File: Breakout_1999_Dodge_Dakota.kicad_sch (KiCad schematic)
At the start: 583 parts, among them J1 Dodge_Con, U1 ACS712xLCTR-20A

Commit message: Another draft check in. Deleted unused "export" files.
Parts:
- removed F10, F11, F12, F13, F14, F15, F16, F17, F18, F19, F20, F21, F22, F23, F24, F25, F26, F27, F28, F29, F30, F31, F32, F33, F34, F35, F36, F37, F38, F39, F4, F40, F41, F42, F43, F44, F45, F46, F47, F48, F49, F5, F50, F51, F52, F53, F54, F55, F56, F57, F58, F59, F6, F60, F61, F62, F63, F64, F65, F66, F67, F68, F69, F7, F70, F71, F72, F73, F74, F75, F76, F77, F78, F79, F8, F80, F81, F82, F83, F84, F85, F86, F87, F88, F89, F9, F90, F91, F92, F93, F94, F95, F96: Fuse_Holder, LCSC_parts:LCSC_C492610_Fuse_holder, symbol Device:R_Small
- removed TP10, TP11, TP12, TP13, TP14, TP15, TP16, TP17, TP18, TP19, TP20, TP21, TP22, TP23, TP24, TP25, TP26, TP27, TP28, TP29, TP30, TP31, TP32, TP33, TP34, TP35, TP36, TP37, TP38, TP39, TP4, TP40, TP41, TP42, TP43, TP44, TP45, TP46, TP47, TP48, TP49, TP5, TP50, TP51, TP52, TP53, TP54, TP55, TP56, TP57, TP58, TP59, TP6, TP60, TP61, TP62, TP63, TP64, TP65, TP66, TP67, TP68, TP69, TP7, TP70, TP71, TP72, TP73, TP74, TP75, TP76, TP77, TP78, TP79, TP8, TP80, TP81, TP82, TP83, TP84, TP85, TP86, TP87, TP88, TP89, TP9, TP90, TP91, TP92, TP93, TP94, TP95, TP96: TestPoint_2Pole, TestPoint:TestPoint_2Pads_Pitch5.08mm_Drill1.3mm, symbol Connector:TestPoint_2Pole
- added F104, F105, F106, F107, F108, F109, F110, F111, F112, F113, F114, F115, F116, F117, F118, F119, F1193, F1194, F1195, F1196, F1197, F120, F121, F122, F123, F124, F125, F126, F127, F128, F129, F130, F131, F132, F201, F202, F203, F204, F205, F206, F207, F208, F209, F210, F211, F212, F213, F214, F215, F216, F217, F218, F219, F220, F221, F222, F223, F224, F225, F226, F227, F228, F229, F230, F231, F232, F301, F302, F303, F304, F305, F306, F307, F308, F309, F310, F311, F312, F313, F314, F315, F316, F317, F318, F319, F320, F321, F322, F323, F324, F325, F326, F327, F328, F329, F330, F331, F332: Fuse_Holder, LCSC_parts:LCSC_C2935870_Fuse_holder, symbol Device:R_Small
- added F1385, F1386, F1387, F1389, F1391, F1392, F1393, F1394, F1395, F1396, F1397, F1399, F1401, F1402, F1403, F1404, F1405, F1407, F1411, F1413: Pig_Con, TestPoint:TestPoint_THTPad_1.5x1.5mm_Drill0.7mm, symbol Connector:TestPoint
- added TP104, TP105, TP106, TP107, TP108, TP109, TP110, TP111, TP112, TP113, TP114, TP115, TP116, TP117, TP118, TP119, TP120, TP121, TP122, TP123, TP124, TP125, TP126, TP127, TP128, TP129, TP130, TP131, TP132, TP201, TP202, TP203, TP204, TP205, TP206, TP207, TP208, TP209, TP210, TP211, TP212, TP213, TP214, TP215, TP216, TP217, TP218, TP219, TP220, TP221, TP222, TP223, TP224, TP225, TP226, TP227, TP228, TP229, TP230, TP231, TP232, TP301, TP302, TP303, TP304, TP305, TP306, TP307, TP308, TP309, TP310, TP311, TP312, TP313, TP314, TP315, TP316, TP317, TP318, TP319, TP320, TP321, TP322, TP323, TP324, TP325, TP326, TP327, TP328, TP329, TP330, TP331, TP332: TestPoint_2Pole, TestPoint:TestPoint_2Pads_Pitch5.08mm_Drill1.3mm, symbol Connector:TestPoint_2Pole
- added U1, U2, U3, U4, U5: ACS712xLCTR-20A, Package_SO:SOIC-8_3.9x4.9mm_P1.27mm, symbol Sensor_Current:ACS712xLCTR-20A
- F101: renamed from F1; footprint LCSC_parts:LCSC_C492610_Fuse_holder -> LCSC_parts:LCSC_C2935870_Fuse_holder; LCSC C492610 -> C2935870
- F102: renamed from F2; footprint LCSC_parts:LCSC_C492610_Fuse_holder -> LCSC_parts:LCSC_C2935870_Fuse_holder; LCSC C492610 -> C2935870
- F103: renamed from F3; footprint LCSC_parts:LCSC_C492610_Fuse_holder -> LCSC_parts:LCSC_C2935870_Fuse_holder; LCSC C492610 -> C2935870
- F1198: renamed from F385; footprint LCSC_parts:LCSC_C492610_Fuse_holder -> LCSC_parts:LCSC_C2935870_Fuse_holder; LCSC C492610 -> C2935870
- F401: renamed from F97; footprint LCSC_parts:LCSC_C492610_Fuse_holder -> LCSC_parts:LCSC_C2935870_Fuse_holder; LCSC C492610 -> C2935870
- F402: renamed from F98; footprint LCSC_parts:LCSC_C492610_Fuse_holder -> LCSC_parts:LCSC_C2935870_Fuse_holder; LCSC C492610 -> C2935870
- F403: renamed from F99; footprint LCSC_parts:LCSC_C492610_Fuse_holder -> LCSC_parts:LCSC_C2935870_Fuse_holder; LCSC C492610 -> C2935870
- F404: renamed from F100; footprint LCSC_parts:LCSC_C492610_Fuse_holder -> LCSC_parts:LCSC_C2935870_Fuse_holder; LCSC C492610 -> C2935870
- F405: renamed from F101; footprint LCSC_parts:LCSC_C492610_Fuse_holder -> LCSC_parts:LCSC_C2935870_Fuse_holder; LCSC C492610 -> C2935870
- F406: renamed from F102; footprint LCSC_parts:LCSC_C492610_Fuse_holder -> LCSC_parts:LCSC_C2935870_Fuse_holder; LCSC C492610 -> C2935870
- F407: renamed from F103; footprint LCSC_parts:LCSC_C492610_Fuse_holder -> LCSC_parts:LCSC_C2935870_Fuse_holder; LCSC C492610 -> C2935870
- F408: renamed from F104; footprint LCSC_parts:LCSC_C492610_Fuse_holder -> LCSC_parts:LCSC_C2935870_Fuse_holder; LCSC C492610 -> C2935870
- F409: renamed from F105; footprint LCSC_parts:LCSC_C492610_Fuse_holder -> LCSC_parts:LCSC_C2935870_Fuse_holder; LCSC C492610 -> C2935870
- F410: renamed from F106; footprint LCSC_parts:LCSC_C492610_Fuse_holder -> LCSC_parts:LCSC_C2935870_Fuse_holder; LCSC C492610 -> C2935870
- F411: renamed from F107; footprint LCSC_parts:LCSC_C492610_Fuse_holder -> LCSC_parts:LCSC_C2935870_Fuse_holder; LCSC C492610 -> C2935870
- F412: renamed from F108; footprint LCSC_parts:LCSC_C492610_Fuse_holder -> LCSC_parts:LCSC_C2935870_Fuse_holder; LCSC C492610 -> C2935870
- F413: renamed from F109; footprint LCSC_parts:LCSC_C492610_Fuse_holder -> LCSC_parts:LCSC_C2935870_Fuse_holder; LCSC C492610 -> C2935870
- F414: renamed from F110; footprint LCSC_parts:LCSC_C492610_Fuse_holder -> LCSC_parts:LCSC_C2935870_Fuse_holder; LCSC C492610 -> C2935870
- F415: renamed from F111; footprint LCSC_parts:LCSC_C492610_Fuse_holder -> LCSC_parts:LCSC_C2935870_Fuse_holder; LCSC C492610 -> C2935870
- F416: renamed from F112; footprint LCSC_parts:LCSC_C492610_Fuse_holder -> LCSC_parts:LCSC_C2935870_Fuse_holder; LCSC C492610 -> C2935870
- F417: renamed from F113; footprint LCSC_parts:LCSC_C492610_Fuse_holder -> LCSC_parts:LCSC_C2935870_Fuse_holder; LCSC C492610 -> C2935870
- F418: renamed from F114; footprint LCSC_parts:LCSC_C492610_Fuse_holder -> LCSC_parts:LCSC_C2935870_Fuse_holder; LCSC C492610 -> C2935870
- F419: renamed from F115; footprint LCSC_parts:LCSC_C492610_Fuse_holder -> LCSC_parts:LCSC_C2935870_Fuse_holder; LCSC C492610 -> C2935870
- F420: renamed from F116; footprint LCSC_parts:LCSC_C492610_Fuse_holder -> LCSC_parts:LCSC_C2935870_Fuse_holder; LCSC C492610 -> C2935870
- F421: renamed from F117; footprint LCSC_parts:LCSC_C492610_Fuse_holder -> LCSC_parts:LCSC_C2935870_Fuse_holder; LCSC C492610 -> C2935870
- F422: renamed from F118; footprint LCSC_parts:LCSC_C492610_Fuse_holder -> LCSC_parts:LCSC_C2935870_Fuse_holder; LCSC C492610 -> C2935870
- F423: renamed from F119; footprint LCSC_parts:LCSC_C492610_Fuse_holder -> LCSC_parts:LCSC_C2935870_Fuse_holder; LCSC C492610 -> C2935870
- F424: renamed from F120; footprint LCSC_parts:LCSC_C492610_Fuse_holder -> LCSC_parts:LCSC_C2935870_Fuse_holder; LCSC C492610 -> C2935870
- F425: renamed from F121; footprint LCSC_parts:LCSC_C492610_Fuse_holder -> LCSC_parts:LCSC_C2935870_Fuse_holder; LCSC C492610 -> C2935870
- F426: renamed from F122; footprint LCSC_parts:LCSC_C492610_Fuse_holder -> LCSC_parts:LCSC_C2935870_Fuse_holder; LCSC C492610 -> C2935870
- F427: renamed from F123; footprint LCSC_parts:LCSC_C492610_Fuse_holder -> LCSC_parts:LCSC_C2935870_Fuse_holder; LCSC C492610 -> C2935870
- F428: renamed from F124; footprint LCSC_parts:LCSC_C492610_Fuse_holder -> LCSC_parts:LCSC_C2935870_Fuse_holder; LCSC C492610 -> C2935870
- F429: renamed from F125; footprint LCSC_parts:LCSC_C492610_Fuse_holder -> LCSC_parts:LCSC_C2935870_Fuse_holder; LCSC C492610 -> C2935870
- F430: renamed from F126; footprint LCSC_parts:LCSC_C492610_Fuse_holder -> LCSC_parts:LCSC_C2935870_Fuse_holder; LCSC C492610 -> C2935870
- F431: renamed from F127; footprint LCSC_parts:LCSC_C492610_Fuse_holder -> LCSC_parts:LCSC_C2935870_Fuse_holder; LCSC C492610 -> C2935870
- F432: renamed from F128; footprint LCSC_parts:LCSC_C492610_Fuse_holder -> LCSC_parts:LCSC_C2935870_Fuse_holder; LCSC C492610 -> C2935870
- F501: renamed from F129; footprint LCSC_parts:LCSC_C492610_Fuse_holder -> LCSC_parts:LCSC_C2935870_Fuse_holder; LCSC C492610 -> C2935870
- F502: renamed from F130; footprint LCSC_parts:LCSC_C492610_Fuse_holder -> LCSC_parts:LCSC_C2935870_Fuse_holder; LCSC C492610 -> C2935870
- F503: renamed from F131; footprint LCSC_parts:LCSC_C492610_Fuse_holder -> LCSC_parts:LCSC_C2935870_Fuse_holder; LCSC C492610 -> C2935870
- F504: renamed from F132; footprint LCSC_parts:LCSC_C492610_Fuse_holder -> LCSC_parts:LCSC_C2935870_Fuse_holder; LCSC C492610 -> C2935870
- F505: renamed from F133; footprint LCSC_parts:LCSC_C492610_Fuse_holder -> LCSC_parts:LCSC_C2935870_Fuse_holder; LCSC C492610 -> C2935870
- F506: renamed from F134; footprint LCSC_parts:LCSC_C492610_Fuse_holder -> LCSC_parts:LCSC_C2935870_Fuse_holder; LCSC C492610 -> C2935870
- F507: renamed from F135; footprint LCSC_parts:LCSC_C492610_Fuse_holder -> LCSC_parts:LCSC_C2935870_Fuse_holder; LCSC C492610 -> C2935870
- F508: renamed from F136; footprint LCSC_parts:LCSC_C492610_Fuse_holder -> LCSC_parts:LCSC_C2935870_Fuse_holder; LCSC C492610 -> C2935870
- F509: renamed from F137; footprint LCSC_parts:LCSC_C492610_Fuse_holder -> LCSC_parts:LCSC_C2935870_Fuse_holder; LCSC C492610 -> C2935870
- F510: renamed from F138; footprint LCSC_parts:LCSC_C492610_Fuse_holder -> LCSC_parts:LCSC_C2935870_Fuse_holder; LCSC C492610 -> C2935870
- F511: renamed from F139; footprint LCSC_parts:LCSC_C492610_Fuse_holder -> LCSC_parts:LCSC_C2935870_Fuse_holder; LCSC C492610 -> C2935870
- F512: renamed from F140; footprint LCSC_parts:LCSC_C492610_Fuse_holder -> LCSC_parts:LCSC_C2935870_Fuse_holder; LCSC C492610 -> C2935870
- F513: renamed from F141; footprint LCSC_parts:LCSC_C492610_Fuse_holder -> LCSC_parts:LCSC_C2935870_Fuse_holder; LCSC C492610 -> C2935870
- F514: renamed from F142; footprint LCSC_parts:LCSC_C492610_Fuse_holder -> LCSC_parts:LCSC_C2935870_Fuse_holder; LCSC C492610 -> C2935870
- F515: renamed from F143; footprint LCSC_parts:LCSC_C492610_Fuse_holder -> LCSC_parts:LCSC_C2935870_Fuse_holder; LCSC C492610 -> C2935870
- F516: renamed from F144; footprint LCSC_parts:LCSC_C492610_Fuse_holder -> LCSC_parts:LCSC_C2935870_Fuse_holder; LCSC C492610 -> C2935870
- F517: renamed from F145; footprint LCSC_parts:LCSC_C492610_Fuse_holder -> LCSC_parts:LCSC_C2935870_Fuse_holder; LCSC C492610 -> C2935870
- F518: renamed from F146; footprint LCSC_parts:LCSC_C492610_Fuse_holder -> LCSC_parts:LCSC_C2935870_Fuse_holder; LCSC C492610 -> C2935870
- F519: renamed from F147; footprint LCSC_parts:LCSC_C492610_Fuse_holder -> LCSC_parts:LCSC_C2935870_Fuse_holder; LCSC C492610 -> C2935870
- F520: renamed from F148; footprint LCSC_parts:LCSC_C492610_Fuse_holder -> LCSC_parts:LCSC_C2935870_Fuse_holder; LCSC C492610 -> C2935870
- F521: renamed from F149; footprint LCSC_parts:LCSC_C492610_Fuse_holder -> LCSC_parts:LCSC_C2935870_Fuse_holder; LCSC C492610 -> C2935870
- F522: renamed from F150; footprint LCSC_parts:LCSC_C492610_Fuse_holder -> LCSC_parts:LCSC_C2935870_Fuse_holder; LCSC C492610 -> C2935870
- F523: renamed from F151; footprint LCSC_parts:LCSC_C492610_Fuse_holder -> LCSC_parts:LCSC_C2935870_Fuse_holder; LCSC C492610 -> C2935870
- F524: renamed from F152; footprint LCSC_parts:LCSC_C492610_Fuse_holder -> LCSC_parts:LCSC_C2935870_Fuse_holder; LCSC C492610 -> C2935870
- F525: renamed from F153; footprint LCSC_parts:LCSC_C492610_Fuse_holder -> LCSC_parts:LCSC_C2935870_Fuse_holder; LCSC C492610 -> C2935870
- F526: renamed from F154; footprint LCSC_parts:LCSC_C492610_Fuse_holder -> LCSC_parts:LCSC_C2935870_Fuse_holder; LCSC C492610 -> C2935870
- F527: renamed from F155; footprint LCSC_parts:LCSC_C492610_Fuse_holder -> LCSC_parts:LCSC_C2935870_Fuse_holder; LCSC C492610 -> C2935870
- F528: renamed from F156; footprint LCSC_parts:LCSC_C492610_Fuse_holder -> LCSC_parts:LCSC_C2935870_Fuse_holder; LCSC C492610 -> C2935870
- F529: renamed from F157; footprint LCSC_parts:LCSC_C492610_Fuse_holder -> LCSC_parts:LCSC_C2935870_Fuse_holder; LCSC C492610 -> C2935870
- F530: renamed from F158; footprint LCSC_parts:LCSC_C492610_Fuse_holder -> LCSC_parts:LCSC_C2935870_Fuse_holder; LCSC C492610 -> C2935870
- F531: renamed from F159; footprint LCSC_parts:LCSC_C492610_Fuse_holder -> LCSC_parts:LCSC_C2935870_Fuse_holder; LCSC C492610 -> C2935870
- F532: renamed from F160; footprint LCSC_parts:LCSC_C492610_Fuse_holder -> LCSC_parts:LCSC_C2935870_Fuse_holder; LCSC C492610 -> C2935870
- F601: renamed from F161; footprint LCSC_parts:LCSC_C492610_Fuse_holder -> LCSC_parts:LCSC_C2935870_Fuse_holder; LCSC C492610 -> C2935870
- F602: renamed from F162; footprint LCSC_parts:LCSC_C492610_Fuse_holder -> LCSC_parts:LCSC_C2935870_Fuse_holder; LCSC C492610 -> C2935870
- F603: renamed from F163; footprint LCSC_parts:LCSC_C492610_Fuse_holder -> LCSC_parts:LCSC_C2935870_Fuse_holder; LCSC C492610 -> C2935870
- F604: renamed from F164; footprint LCSC_parts:LCSC_C492610_Fuse_holder -> LCSC_parts:LCSC_C2935870_Fuse_holder; LCSC C492610 -> C2935870
- F605: renamed from F165; footprint LCSC_parts:LCSC_C492610_Fuse_holder -> LCSC_parts:LCSC_C2935870_Fuse_holder; LCSC C492610 -> C2935870
- F606: renamed from F166; footprint LCSC_parts:LCSC_C492610_Fuse_holder -> LCSC_parts:LCSC_C2935870_Fuse_holder; LCSC C492610 -> C2935870
- F607: renamed from F167; footprint LCSC_parts:LCSC_C492610_Fuse_holder -> LCSC_parts:LCSC_C2935870_Fuse_holder; LCSC C492610 -> C2935870
- F608: renamed from F168; footprint LCSC_parts:LCSC_C492610_Fuse_holder -> LCSC_parts:LCSC_C2935870_Fuse_holder; LCSC C492610 -> C2935870
- F609: renamed from F169; footprint LCSC_parts:LCSC_C492610_Fuse_holder -> LCSC_parts:LCSC_C2935870_Fuse_holder; LCSC C492610 -> C2935870
- F610: renamed from F170; footprint LCSC_parts:LCSC_C492610_Fuse_holder -> LCSC_parts:LCSC_C2935870_Fuse_holder; LCSC C492610 -> C2935870
- F611: renamed from F171; footprint LCSC_parts:LCSC_C492610_Fuse_holder -> LCSC_parts:LCSC_C2935870_Fuse_holder; LCSC C492610 -> C2935870
- F612: renamed from F172; footprint LCSC_parts:LCSC_C492610_Fuse_holder -> LCSC_parts:LCSC_C2935870_Fuse_holder; LCSC C492610 -> C2935870
- F613: renamed from F173; footprint LCSC_parts:LCSC_C492610_Fuse_holder -> LCSC_parts:LCSC_C2935870_Fuse_holder; LCSC C492610 -> C2935870
- F614: renamed from F174; footprint LCSC_parts:LCSC_C492610_Fuse_holder -> LCSC_parts:LCSC_C2935870_Fuse_holder; LCSC C492610 -> C2935870
- F615: renamed from F175; footprint LCSC_parts:LCSC_C492610_Fuse_holder -> LCSC_parts:LCSC_C2935870_Fuse_holder; LCSC C492610 -> C2935870
- F616: renamed from F176; footprint LCSC_parts:LCSC_C492610_Fuse_holder -> LCSC_parts:LCSC_C2935870_Fuse_holder; LCSC C492610 -> C2935870
- F617: renamed from F177; footprint LCSC_parts:LCSC_C492610_Fuse_holder -> LCSC_parts:LCSC_C2935870_Fuse_holder; LCSC C492610 -> C2935870
- F618: renamed from F178; footprint LCSC_parts:LCSC_C492610_Fuse_holder -> LCSC_parts:LCSC_C2935870_Fuse_holder; LCSC C492610 -> C2935870
- F619: renamed from F179; footprint LCSC_parts:LCSC_C492610_Fuse_holder -> LCSC_parts:LCSC_C2935870_Fuse_holder; LCSC C492610 -> C2935870
- F620: renamed from F180; footprint LCSC_parts:LCSC_C492610_Fuse_holder -> LCSC_parts:LCSC_C2935870_Fuse_holder; LCSC C492610 -> C2935870
- F621: renamed from F181; footprint LCSC_parts:LCSC_C492610_Fuse_holder -> LCSC_parts:LCSC_C2935870_Fuse_holder; LCSC C492610 -> C2935870
- F622: renamed from F182; footprint LCSC_parts:LCSC_C492610_Fuse_holder -> LCSC_parts:LCSC_C2935870_Fuse_holder; LCSC C492610 -> C2935870
- F623: renamed from F183; footprint LCSC_parts:LCSC_C492610_Fuse_holder -> LCSC_parts:LCSC_C2935870_Fuse_holder; LCSC C492610 -> C2935870
- F624: renamed from F184; footprint LCSC_parts:LCSC_C492610_Fuse_holder -> LCSC_parts:LCSC_C2935870_Fuse_holder; LCSC C492610 -> C2935870
- F625: renamed from F185; footprint LCSC_parts:LCSC_C492610_Fuse_holder -> LCSC_parts:LCSC_C2935870_Fuse_holder; LCSC C492610 -> C2935870
- F626: renamed from F186; footprint LCSC_parts:LCSC_C492610_Fuse_holder -> LCSC_parts:LCSC_C2935870_Fuse_holder; LCSC C492610 -> C2935870
- F627: renamed from F187; footprint LCSC_parts:LCSC_C492610_Fuse_holder -> LCSC_parts:LCSC_C2935870_Fuse_holder; LCSC C492610 -> C2935870
- F628: renamed from F188; footprint LCSC_parts:LCSC_C492610_Fuse_holder -> LCSC_parts:LCSC_C2935870_Fuse_holder; LCSC C492610 -> C2935870
- F629: renamed from F189; footprint LCSC_parts:LCSC_C492610_Fuse_holder -> LCSC_parts:LCSC_C2935870_Fuse_holder; LCSC C492610 -> C2935870
- F630: renamed from F190; footprint LCSC_parts:LCSC_C492610_Fuse_holder -> LCSC_parts:LCSC_C2935870_Fuse_holder; LCSC C492610 -> C2935870
- F631: renamed from F191; footprint LCSC_parts:LCSC_C492610_Fuse_holder -> LCSC_parts:LCSC_C2935870_Fuse_holder; LCSC C492610 -> C2935870
- F632: renamed from F192; footprint LCSC_parts:LCSC_C492610_Fuse_holder -> LCSC_parts:LCSC_C2935870_Fuse_holder; LCSC C492610 -> C2935870
- renumbered F193 to F1001, F194 to F1002, F195 to F1003, F196 to F1004, F197 to F1005, F198 to F1006, F199 to F1007, F200 to F1008, F201 to F1009, F202 to F1010, F203 to F1011, F204 to F1012, F205 to F1013, F206 to F1014, F207 to F1015, F208 to F1016, F209 to F1017, F210 to F1018, F211 to F1019, F212 to F1020, F213 to F1021, F214 to F1022, F215 to F1023, F216 to F1024, F217 to F1025, F218 to F1026, F219 to F1027, F220 to F1028, F221 to F1029, F222 to F1030, F223 to F1031, F224 to F1032, F225 to F1033, F226 to F1034, F227 to F1035, F228 to F1036, F229 to F1037, F230 to F1038, F231 to F1039, F232 to F1040, F233 to F1041, F234 to F1042, F235 to F1043, F236 to F1044, F237 to F1045, F238 to F1046, F239 to F1047, F240 to F1048, F241 to F1049, F242 to F1050, F243 to F1051, F244 to F1052, F245 to F1053, F246 to F1054, F247 to F1055, F248 to F1056, F249 to F1057, F250 to F1058, F251 to F1059, F252 to F1060, F253 to F1061, F254 to F1062, F255 to F1063, F256 to F1064, F257 to F1065, F258 to F1066, F259 to F1067, F260 to F1068, F261 to F1069, F262 to F1070, F263 to F1071, F264 to F1072, F265 to F1073, F266 to F1074, F267 to F1075, F268 to F1076, F269 to F1077, F270 to F1078, F271 to F1079, F272 to F1080, F273 to F1081, F274 to F1082, F275 to F1083, F276 to F1084, F277 to F1085, F278 to F1086, F279 to F1087, F280 to F1088, F281 to F1089, F282 to F1090, F283 to F1091, F284 to F1092, F285 to F1093, F286 to F1094, F287 to F1095, F288 to F1096, F289 to F1097, F290 to F1098, F291 to F1099, F292 to F1100, F293 to F1101, F294 to F1102, F295 to F1103, F296 to F1104, F297 to F1105, F298 to F1106, F299 to F1107, F300 to F1108, F301 to F1109, F302 to F1110, F303 to F1111, F304 to F1112, F305 to F1113, F306 to F1114, F307 to F1115, F308 to F1116, F309 to F1117, F310 to F1118, F311 to F1119, F312 to F1120, F313 to F1121, F314 to F1122, F315 to F1123, F316 to F1124, F317 to F1125, F318 to F1126, F319 to F1127, F320 to F1128, F321 to F1129, F322 to F1130, F323 to F1131, F324 to F1132, F325 to F1133, F326 to F1134, F327 to F1135, F328 to F1136, F329 to F1137, F330 to F1138, F331 to F1139, F332 to F1140, F333 to F1141, F334 to F1142, F335 to F1143, F336 to F1144, F337 to F1145, F338 to F1146, F339 to F1147, F340 to F1148, F341 to F1149, F342 to F1150, F343 to F1151, F344 to F1152, F345 to F1153, F346 to F1154, F347 to F1155, F348 to F1156, F349 to F1157, F350 to F1158, F351 to F1159, F352 to F1160, F353 to F1161, F354 to F1162, F355 to F1163, F356 to F1164, F357 to F1165, F358 to F1166, F359 to F1167, F360 to F1168, F361 to F1169, F362 to F1170, F363 to F1171, F364 to F1172, F365 to F1173, F366 to F1174, F367 to F1175, F368 to F1176, F369 to F1177, F370 to F1178, F371 to F1179, F372 to F1180, F373 to F1181, F374 to F1182, F375 to F1183, F376 to F1184, F377 to F1185, F378 to F1186, F379 to F1187, F380 to F1188, F381 to F1189, F382 to F1190, F383 to F1191, F384 to F1192, F386 to F1406, F388 to F1409, F389 to F1412, F387 to F1414, TP1 to TP101, TP2 to TP102, TP3 to TP103, TP97 to TP401, TP98 to TP402, TP99 to TP403, TP100 to TP404, TP101 to TP405, TP102 to TP406, TP103 to TP407, TP104 to TP408, TP105 to TP409, TP106 to TP410, TP107 to TP411, TP108 to TP412, TP109 to TP413, TP110 to TP414, TP111 to TP415, TP112 to TP416, TP113 to TP417, TP114 to TP418, TP115 to TP419, TP116 to TP420, TP117 to TP421, TP118 to TP422, TP119 to TP423, TP120 to TP424, TP121 to TP425, TP122 to TP426, TP123 to TP427, TP124 to TP428, TP125 to TP429, TP126 to TP430, TP127 to TP431, TP128 to TP432, TP129 to TP501, TP130 to TP502, TP131 to TP503, TP132 to TP504, TP133 to TP505, TP134 to TP506, TP135 to TP507, TP136 to TP508, TP137 to TP509, TP138 to TP510, TP139 to TP511, TP140 to TP512, TP141 to TP513, TP142 to TP514, TP143 to TP515, TP144 to TP516, TP145 to TP517, TP146 to TP518, TP147 to TP519, TP148 to TP520, TP149 to TP521, TP150 to TP522, TP151 to TP523, TP152 to TP524, TP153 to TP525, TP154 to TP526, TP155 to TP527, TP156 to TP528, TP157 to TP529, TP158 to TP530, TP159 to TP531, TP160 to TP532, TP161 to TP601, TP162 to TP602, TP163 to TP603, TP164 to TP604, TP165 to TP605, TP166 to TP606, TP167 to TP607, TP168 to TP608, TP169 to TP609, TP170 to TP610, TP171 to TP611, TP172 to TP612, TP173 to TP613, TP174 to TP614, TP175 to TP615, TP176 to TP616, TP177 to TP617, TP178 to TP618, TP179 to TP619, TP180 to TP620, TP181 to TP621, TP182 to TP622, TP183 to TP623, TP184 to TP624, TP185 to TP625, TP186 to TP626, TP187 to TP627, TP188 to TP628, TP189 to TP629, TP190 to TP630, TP191 to TP631, TP192 to TP632, U1 to U6
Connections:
- net at F616.1, J1.c3-16 (Pin_16): now also F316.2
- net at F432.1, J1.c1-32 (Pin_32): now also F132.2
- net at F526.1, J1.c2-26 (Pin_26): now also F226.2
- net at F423.1, J1.c1-23 (Pin_23): now also F123.2
- net at F610.1, J1.c3-10 (Pin_10): now also F310.2
- net at F501.1, J1.c2-1 (Pin_1): now also F201.2
- net at F414.1, J1.c1-14 (Pin_14): now also F114.2
- net at F430.1, J1.c1-30 (Pin_30): now also F130.2
- net at F614.1, J1.c3-14 (Pin_14): now also F314.2
- net at F622.1, J1.c3-22 (Pin_22): now also F322.2
- net at F516.1, J1.c2-16 (Pin_16): now also F216.2
- net at F521.1, J1.c2-21 (Pin_21): now also F221.2
- net at F428.1, J1.c1-28 (Pin_28): now also F128.2
- net at F431.1, J1.c1-31 (Pin_31): now also F131.2
- net at F617.1, J1.c3-17 (Pin_17): now also F317.2
- net at F509.1, J1.c2-9 (Pin_9): now also F209.2
- net at F621.1, J1.c3-21 (Pin_21): now also F321.2
- net at F631.1, J1.c3-31 (Pin_31): now also F331.2
- net at F529.1, J1.c2-29 (Pin_29): now also F229.2
- net at F619.1, J1.c3-19 (Pin_19): now also F319.2
- net at F531.1, J1.c2-31 (Pin_31): now also F231.2
- net at F525.1, J1.c2-25 (Pin_25): now also F225.2
- net at F605.1, J1.c3-5 (Pin_5): now also F305.2
- net at F418.1, J1.c1-18 (Pin_18): now also F118.2
- net at F515.1, J1.c2-15 (Pin_15): now also F215.2
- net at F407.1, J1.c1-7 (Pin_7): now also F107.2
- net at F510.1, J1.c2-10 (Pin_10): now also F210.2
- net at F512.1, J1.c2-12 (Pin_12): now also F212.2
- net at F411.1, J1.c1-11 (Pin_11): now also F111.2
- net at F601.1, J1.c3-1 (Pin_1): now also F301.2
- net at F519.1, J1.c2-19 (Pin_19): now also F219.2
- net at F416.1, J1.c1-16 (Pin_16): now also F116.2
- net at F527.1, J1.c2-27 (Pin_27): now also F227.2
- net at F629.1, J1.c3-29 (Pin_29): now also F329.2
- net at F421.1, J1.c1-21 (Pin_21): now also F121.2
- net at F602.1, J1.c3-2 (Pin_2): now also F302.2
- net at F424.1, J1.c1-24 (Pin_24): now also F124.2
- net at F429.1, J1.c1-29 (Pin_29): now also F129.2
- net at F623.1, J1.c3-23 (Pin_23): now also F323.2
- net at F523.1, J1.c2-23 (Pin_23): now also F223.2
- net at F532.1, J1.c2-32 (Pin_32): now also F232.2
- net at F413.1, J1.c1-13 (Pin_13): now also F113.2
- net at F530.1, J1.c2-30 (Pin_30): now also F230.2
- net at F615.1, J1.c3-15 (Pin_15): now also F315.2
- net at F608.1, J1.c3-8 (Pin_8): now also F308.2
- net at F409.1, J1.c1-9 (Pin_9): now also F109.2
- net at F506.1, J1.c2-6 (Pin_6): now also F206.2
- net at F422.1, J1.c1-22 (Pin_22): now also F122.2
- net at F609.1, J1.c3-9 (Pin_9): now also F309.2
- net at F410.1, J1.c1-10 (Pin_10): now also F110.2
- net at F420.1, J1.c1-20 (Pin_20): now also F120.2
- net at F425.1, J1.c1-25 (Pin_25): now also F125.2
- net at F507.1, J1.c2-7 (Pin_7): now also F207.2
- net at F611.1, J1.c3-11 (Pin_11): now also F311.2
- net at F630.1, J1.c3-30 (Pin_30): now also F330.2
- net at F518.1, J1.c2-18 (Pin_18): now also F218.2
- net at F419.1, J1.c1-19 (Pin_19): now also F119.2
- net at F513.1, J1.c2-13 (Pin_13): now also F213.2
- net at F607.1, J1.c3-7 (Pin_7): now also F307.2
- net at F406.1, J1.c1-6 (Pin_6): now also F106.2
- net at F632.1, J1.c3-32 (Pin_32): now also F332.2
- net at F511.1, J1.c2-11 (Pin_11): now also F211.2
- net at F417.1, J1.c1-17 (Pin_17): now also F117.2
- net at F514.1, J1.c2-14 (Pin_14): now also F214.2
- net at F517.1, J1.c2-17 (Pin_17): now also F217.2
- net at F502.1, J1.c2-2 (Pin_2): now also F202.2
- net at F520.1, J1.c2-20 (Pin_20): now also F220.2
- net at F522.1, J1.c2-22 (Pin_22): now also F222.2
- net at F524.1, J1.c2-24 (Pin_24): now also F224.2
- net at F528.1, J1.c2-28 (Pin_28): now also F228.2
- net at F503.1, J1.c2-3 (Pin_3): now also F203.2
- net at F504.1, J1.c2-4 (Pin_4): now also F204.2
- net at F505.1, J1.c2-5 (Pin_5): now also F205.2
- net at F508.1, J1.c2-8 (Pin_8): now also F208.2
- net at F620.1, J1.c3-20 (Pin_20): now also F320.2
- net at F606.1, J1.c3-6 (Pin_6): now also F306.2
- net at F408.1, J1.c1-8 (Pin_8): now also F108.2
- net at F627.1, J1.c3-27 (Pin_27): now also F327.2
- net at F604.1, J1.c3-4 (Pin_4): now also F304.2
- net at F626.1, J1.c3-26 (Pin_26): now also F326.2
- net at F404.1, J1.c1-4 (Pin_4): now also F104.2
- net at F412.1, J1.c1-12 (Pin_12): now also F112.2
- net at F415.1, J1.c1-15 (Pin_15): now also F115.2
- net at F426.1, J1.c1-26 (Pin_26): now also F126.2
- net at F427.1, J1.c1-27 (Pin_27): now also F127.2
- net at F405.1, J1.c1-5 (Pin_5): now also F105.2
- net at F613.1, J1.c3-13 (Pin_13): now also F313.2
- net at F625.1, J1.c3-25 (Pin_25): now also F325.2
- net at F624.1, J1.c3-24 (Pin_24): now also F324.2
- net at F628.1, J1.c3-28 (Pin_28): now also F328.2
- net at F612.1, J1.c3-12 (Pin_12): now also F312.2
- net at F618.1, J1.c3-18 (Pin_18): now also F318.2
- net at F603.1, J1.c3-3 (Pin_3): now also F303.2
- new net: F1197.1, U5.3 (IP-), U5.4 (IP-)
- new net: F1197.2, U5.1 (IP+), U5.2 (IP+)
- new net: F313.1, TP313.1, TP313.2
- new net: F112.1, TP112.1, TP112.2
- new net: F1385.1, U1.8 (VCC)
- new net: F127.1, TP127.1, TP127.2
- new net: F107.1, TP107.1, TP107.2
- new net: F206.1, TP206.1, TP206.2
- new net: F116.1, TP116.1, TP116.2
- new net: F1401.1, U3.6 (FILTER)
- new net: F108.1, TP108.1, TP108.2
- new net: F211.1, TP211.1, TP211.2
- new net: F330.1, TP330.1, TP330.2
- new net: F217.1, TP217.1, TP217.2
- new net: F226.1, TP226.1, TP226.2
- new net: F310.1, TP310.1, TP310.2
- new net: F1193.1, U1.3 (IP-), U1.4 (IP-)
- new net: F1193.2, U1.1 (IP+), U1.2 (IP+)
- new net: F121.1, TP121.1, TP121.2
- new net: F120.1, TP120.1, TP120.2
- new net: F1404.1, U4.5 (GND)
- new net: F1407.1, U5.7 (VIOUT)
- new net: F1389.1, U2.7 (VIOUT)
- new net: F209.1, TP209.1, TP209.2
- new net: F203.1, TP203.1, TP203.2
- new net: F204.1, TP204.1, TP204.2
- new net: F216.1, TP216.1, TP216.2
- new net: F123.1, TP123.1, TP123.2
- new net: F131.1, TP131.1, TP131.2
- new net: F301.1, TP301.1, TP301.2
- new net: F231.1, TP231.1, TP231.2
- new net: F312.1, TP312.1, TP312.2
- new net: F331.1, TP331.1, TP331.2
- new net: F126.1, TP126.1, TP126.2
- new net: F125.1, TP125.1, TP125.2
- new net: F327.1, TP327.1, TP327.2
- new net: F221.1, TP221.1, TP221.2
- new net: F110.1, TP110.1, TP110.2
- new net: F1196.2, U4.1 (IP+), U4.2 (IP+)
- new net: F1196.1, U4.3 (IP-), U4.4 (IP-)
- new net: F1402.1, U4.6 (FILTER)
- new net: F1399.1, U4.7 (VIOUT)
- new net: F1396.1, U4.8 (VCC)
- new net: F220.1, TP220.1, TP220.2
- new net: F315.1, TP315.1, TP315.2
- new net: F323.1, TP323.1, TP323.2
- new net: F117.1, TP117.1, TP117.2
- new net: F128.1, TP128.1, TP128.2
- new net: F1395.1, U3.8 (VCC)
- new net: F329.1, TP329.1, TP329.2
- new net: F228.1, TP228.1, TP228.2
- new net: F1194.2, U2.1 (IP+), U2.2 (IP+)
- new net: F1194.1, U2.3 (IP-), U2.4 (IP-)
- new net: F1394.1, U2.5 (GND)
- new net: F1392.1, U2.6 (FILTER)
- new net: F1386.1, U2.8 (VCC)
- new net: F306.1, TP306.1, TP306.2
- new net: F106.1, TP106.1, TP106.2
- new net: F130.1, TP130.1, TP130.2
- new net: F115.1, TP115.1, TP115.2
- new net: F227.1, TP227.1, TP227.2
- new net: F321.1, TP321.1, TP321.2
- new net: F316.1, TP316.1, TP316.2
- new net: F207.1, TP207.1, TP207.2
- new net: F324.1, TP324.1, TP324.2
- new net: F311.1, TP311.1, TP311.2
- new net: F232.1, TP232.1, TP232.2
- new net: F214.1, TP214.1, TP214.2
- new net: F229.1, TP229.1, TP229.2
- new net: F1391.1, U1.6 (FILTER)
- new net: F201.1, TP201.1, TP201.2
- new net: F119.1, TP119.1, TP119.2
- new net: F1393.1, U1.5 (GND)
- new net: F219.1, TP219.1, TP219.2
- new net: F303.1, TP303.1, TP303.2
- new net: F318.1, TP318.1, TP318.2
- new net: F129.1, TP129.1, TP129.2
- new net: F118.1, TP118.1, TP118.2
- new net: F222.1, TP222.1, TP222.2
- new net: F122.1, TP122.1, TP122.2
- new net: F1413.1, U5.5 (GND)
- new net: F317.1, TP317.1, TP317.2
- new net: F230.1, TP230.1, TP230.2
- new net: F332.1, TP332.1, TP332.2
- new net: F1195.2, U3.1 (IP+), U3.2 (IP+)
- new net: F1195.1, U3.3 (IP-), U3.4 (IP-)
- new net: F1403.1, U3.5 (GND)
- new net: F1397.1, U3.7 (VIOUT)
- new net: F109.1, TP109.1, TP109.2
- new net: F309.1, TP309.1, TP309.2
- new net: F208.1, TP208.1, TP208.2
- new net: F314.1, TP314.1, TP314.2
- new net: F322.1, TP322.1, TP322.2
- new net: F308.1, TP308.1, TP308.2
- new net: F319.1, TP319.1, TP319.2
- new net: F328.1, TP328.1, TP328.2
- new net: F114.1, TP114.1, TP114.2
- new net: F224.1, TP224.1, TP224.2
- new net: F210.1, TP210.1, TP210.2
- new net: F307.1, TP307.1, TP307.2
- new net: F325.1, TP325.1, TP325.2
- new net: F326.1, TP326.1, TP326.2
- new net: F113.1, TP113.1, TP113.2
- new net: F124.1, TP124.1, TP124.2
- new net: F202.1, TP202.1, TP202.2
- new net: F302.1, TP302.1, TP302.2
- new net: F104.1, TP104.1, TP104.2
- new net: F213.1, TP213.1, TP213.2
- new net: F225.1, TP225.1, TP225.2
- new net: F111.1, TP111.1, TP111.2
- new net: F212.1, TP212.1, TP212.2
- new net: F304.1, TP304.1, TP304.2
- new net: F223.1, TP223.1, TP223.2
- new net: F105.1, TP105.1, TP105.2
- new net: F132.1, TP132.1, TP132.2
- new net: F1387.1, U1.7 (VIOUT)
- new net: F320.1, TP320.1, TP320.2
- new net: F215.1, TP215.1, TP215.2
- new net: F305.1, TP305.1, TP305.2
- new net: F218.1, TP218.1, TP218.2
- new net: F1405.1, U5.8 (VCC)
- new net: F1411.1, U5.6 (FILTER)
- new net: F205.1, TP205.1, TP205.2
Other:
- moved on the sheet: F1198, F1406, F1409, F1412, F1414, U6

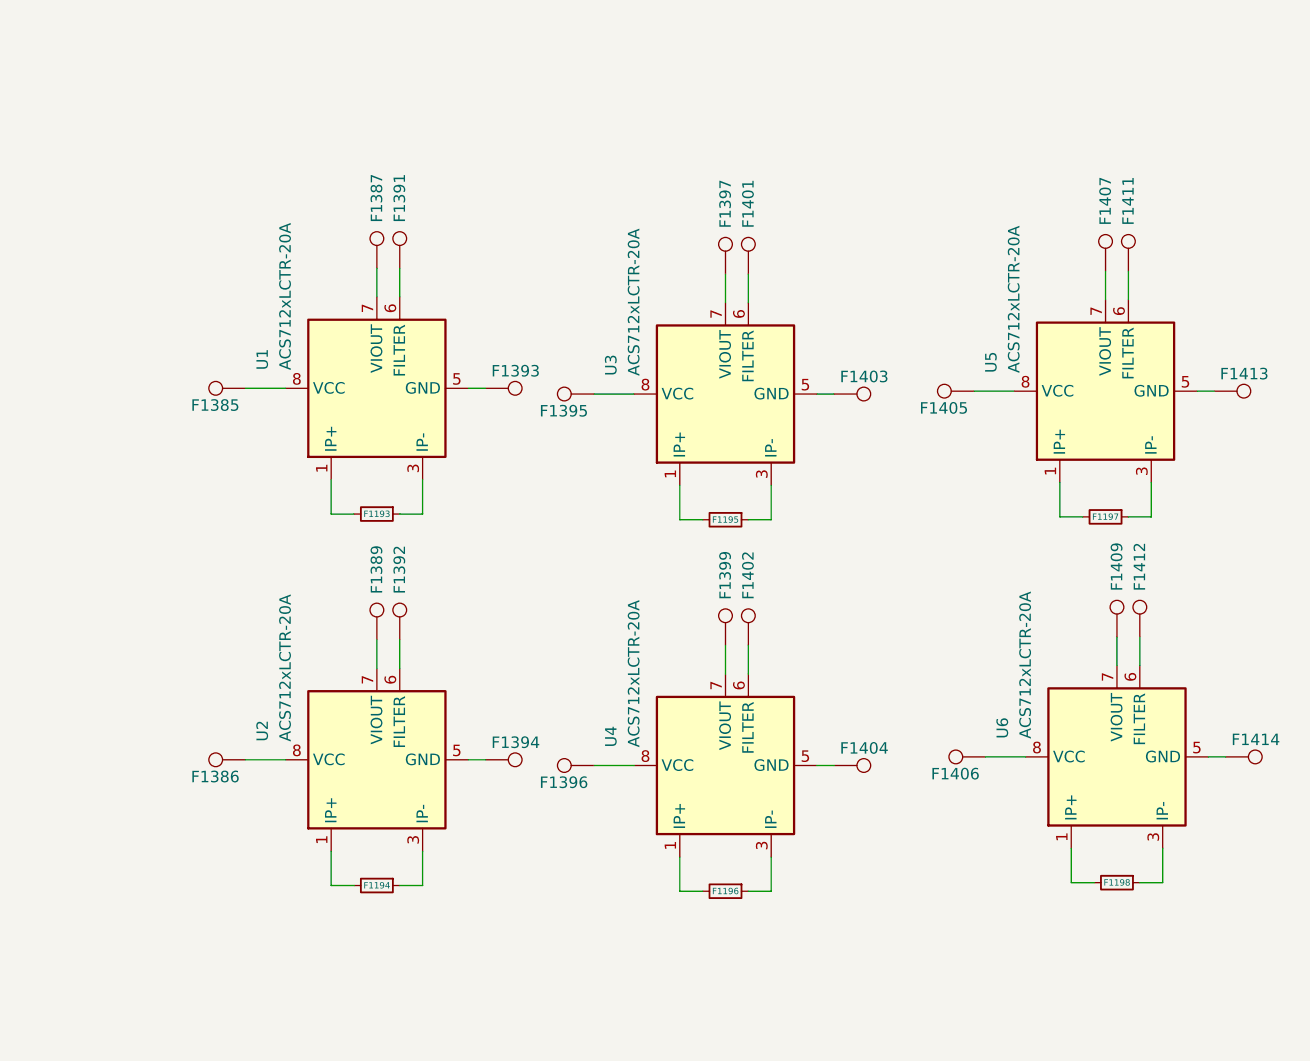
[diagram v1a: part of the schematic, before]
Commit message: Draft commit, mostly routed, silk screen needs work. Passes ERC and DRC
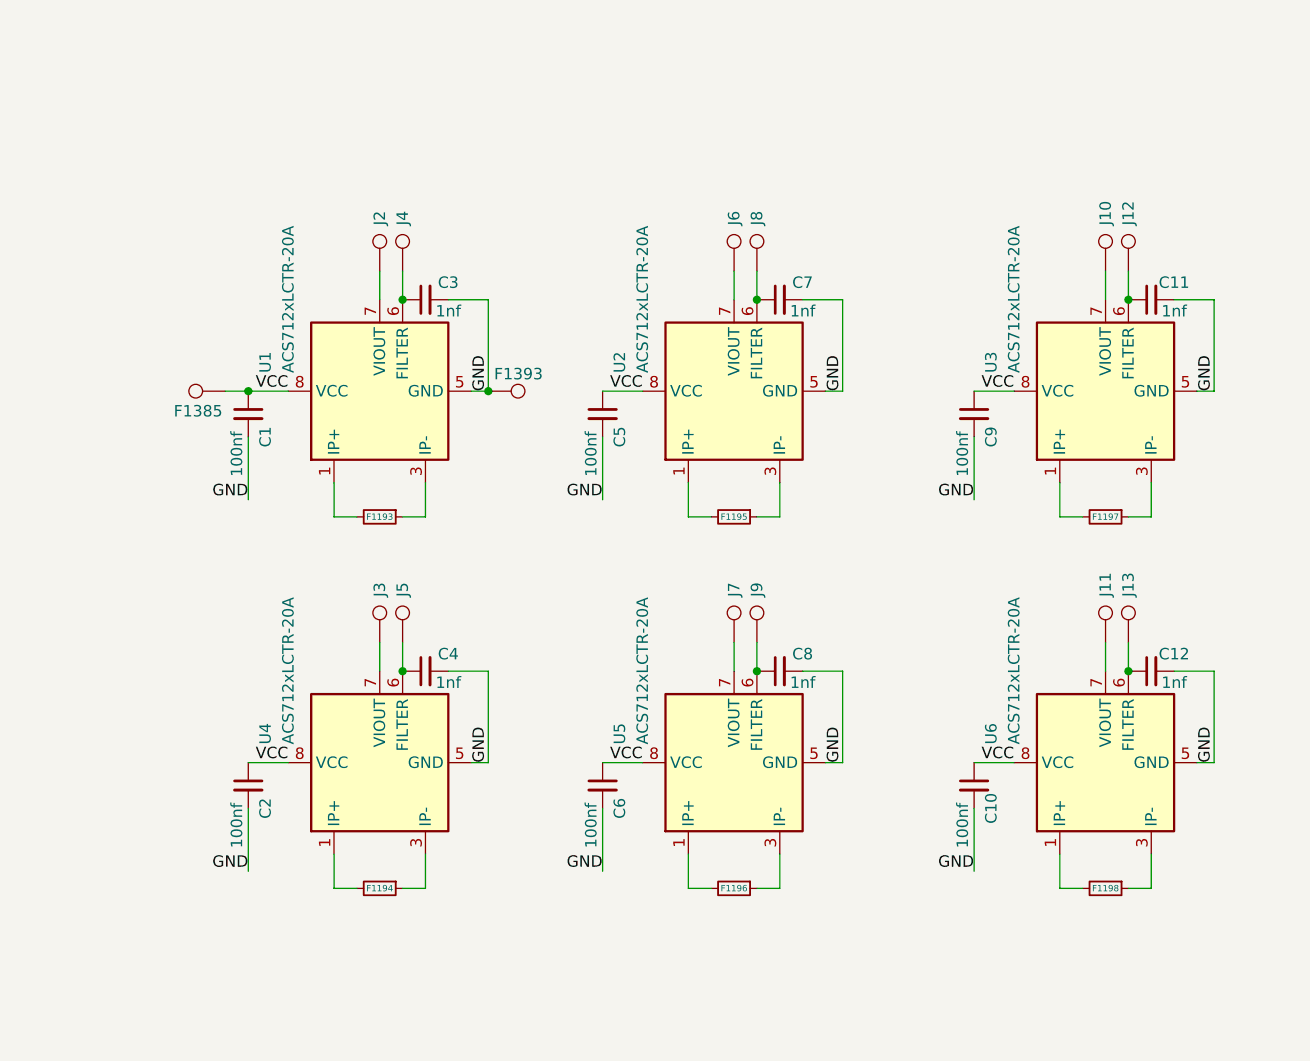
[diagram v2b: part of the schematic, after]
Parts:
- removed F1386, F1394, F1395, F1396, F1403, F1404, F1405, F1406, F1413, F1414: Pig_Con, TestPoint:TestPoint_THTPad_1.5x1.5mm_Drill0.7mm, symbol Connector:TestPoint
- added C1, C10, C2, C5, C6, C9: 100nf, Capacitor_SMD:C_0805_2012Metric, symbol Device:C_Small
- added C11, C12, C3, C4, C7, C8: 1nf, Capacitor_SMD:C_0805_2012Metric, symbol Device:C_Small
- renumbered F1407 to J10, F1409 to J11, F1411 to J12, F1412 to J13, F1387 to J2, F1389 to J3, F1391 to J4, F1392 to J5, F1397 to J6, F1399 to J7, F1401 to J8, F1402 to J9, U3 to U2, U5 to U3, U2 to U4, U4 to U5
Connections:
- net GND: now reaches U6.5 (GND)
- net GND: now also F1393.1, U1.5 (GND), U2.5 (GND), U3.5 (GND), U4.5 (GND), U5.5 (GND), C1.2, C10.2, C11.2, C12.2, C2.2, C3.2, C4.2, C5.2, C6.2, C7.2, C8.2, C9.2
- net VCC: now reaches F1385.1, U1.8 (VCC)
- net VCC: now also U2.8 (VCC), U3.8 (VCC), U4.8 (VCC), U5.8 (VCC), U6.8 (VCC), C1.1, C10.1, C2.1, C5.1, C6.1, C9.1
- net at J8.1, U2.6 (FILTER): now also C7.1
- net at J13.1, U6.6 (FILTER): now also C12.1
- net at J9.1, U5.6 (FILTER): now also C8.1
- net at J5.1, U4.6 (FILTER): now also C4.1
- net at J4.1, U1.6 (FILTER): now also C3.1
- net at J12.1, U3.6 (FILTER): now also C11.1
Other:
- moved on the sheet: F1195, F1196, F1198, F1385, J11, J13, J6, J7, J8, J9, U2, U5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
